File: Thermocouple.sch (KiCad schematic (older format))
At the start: 20 parts, among them P2 CONN_2, P3 CONN_3X2, U2 MCP3901, U3 LMT84, U4 OPA4170

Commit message: Terminal Blocks and ATX Connector
Created footprints for 12pin, 3pin terminal blocks and 24pin ATX Header.
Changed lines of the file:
@@
 	6700 4550 6200 4550
 Wire Wire Line
-	4300 3350 5300 3350
-Wire Wire Line
-	5300 3350 5450 3350
-Wire Wire Line
-	5300 2200 5300 3350
-Wire Wire Line
-	5300 3350 5300 3700
+	4300 3350 5450 3350
+Wire Wire Line
+	5300 2200 5300 3700
 Wire Wire Line
 	5700 2200 5300 2200
@@
 Connection ~ 7550 4550
 Wire Wire Line
-	8600 3650 8600 4200
-Wire Wire Line
-	8600 4200 8600 4450
+	8600 3650 8600 4450
 Wire Wire Line
 	7550 3650 8600 3650
@@
 	8600 3000 8600 2300
 Wire Wire Line
-	7550 3000 8250 3000
-Wire Wire Line
-	8250 3000 8600 3000
-Wire Wire Line
-	7200 2200 7550 2200
-Wire Wire Line
-	7550 2200 7600 2200
+	7550 3000 8600 3000
+Wire Wire Line
+	7200 2200 7600 2200
 Wire Wire Line
 	7550 2400 7550 2200
@@
 	7550 3650 7550 3750
 Wire Wire Line
-	7200 4550 7550 4550
-Wire Wire Line
-	7550 4550 7600 4550
+	7200 4550 7600 4550
 Wire Wire Line
 	7550 4250 7550 4550
@@
 $EndComp
 Wire Wire Line
-	5300 4100 5300 4550
-Wire Wire Line
-	5300 4550 5300 4700
+	5300 4100 5300 4700
 $Comp
 L AGND #PWR09
@@
 	8250 3350 8400 3350
 Wire Wire Line
-	8250 3000 8250 3250
-Wire Wire Line
-	8250 3250 8250 3350
-Wire Wire Line
-	8250 3350 8250 3450
+	8250 3000 8250 3450
 Connection ~ 8250 3000
 $Comp
@@
 	9550 4200 9550 4050
 Wire Wire Line
-	8600 4200 9300 4200
-Wire Wire Line
-	9300 4200 9550 4200
-Wire Wire Line
-	9550 4200 9800 4200
+	8600 4200 9800 4200
 Connection ~ 8600 4200
 Wire Wire Line
@@
 $EndComp
 Wire Wire Line
-	5950 6650 5950 6800
-Wire Wire Line
-	5950 6800 5950 6900
+	5950 6650 5950 6900
 Wire Wire Line
 	5850 6650 5850 6800
 Wire Wire Line
-	5850 6800 5950 6800
-Wire Wire Line
-	5950 6800 6050 6800
-Wire Wire Line
-	6050 6800 6550 6800
+	5850 6800 6550 6800
 Connection ~ 5950 6800
 Wire Wire Line
@@
 $EndComp
 Wire Wire Line
-	5900 5250 5900 5300
-Wire Wire Line
-	5900 5300 5900 5400
+	5900 5250 5900 5400
 $Comp
 L C C10
@@
 $EndComp
 Wire Wire Line
-	2950 1100 2950 1150
-Wire Wire Line
-	2950 1150 2950 1250
+	2950 1100 2950 1250
 Text GLabel 4450 1800 2    60   Input ~ 0
 REF+
@@
 $EndComp
 Wire Wire Line
-	2500 1100 2500 1150
-Wire Wire Line
-	2500 1150 2500 1250
+	2500 1100 2500 1250
 $Comp
 L C C6

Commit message: Layout v1.0
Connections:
- net +12V: no longer U4.4 (V+), U4.4 (V+), U4.4 (V+)
- net -12V: no longer U4.11 (V-), U4.11 (V-), U4.11 (V-)
- new net FE_V+: U4.4 (V+), U4.4 (V+), U4.4 (V+)
- new net FE_V-: U4.11 (V-), U4.11 (V-), U4.11 (V-)
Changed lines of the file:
@@
 Sheet 3 9
 Title ""
-Date "28 feb 2014"
+Date "3 mar 2014"
 Rev ""
 Comp ""
@@
 	8200 4950 8200 5050
 $Comp
-L +12V #PWR015
-U 1 1 530970D9
-P 8200 5050
-F 0 "#PWR015" H 8200 5000 20  0001 C CNN
-F 1 "+12V" H 8200 5150 30  0000 C CNN
-F 2 "" H 8200 5050 60  0000 C CNN
-F 3 "" H 8200 5050 60  0000 C CNN
-	1    8200 5050
-	-1   0    0    1
-$EndComp
-$Comp
-L +12V #PWR016
-U 1 1 530970DF
-P 6050 3850
-F 0 "#PWR016" H 6050 3800 20  0001 C CNN
-F 1 "+12V" H 6050 3950 30  0000 C CNN
-F 2 "" H 6050 3850 60  0000 C CNN
-F 3 "" H 6050 3850 60  0000 C CNN
-	1    6050 3850
-	-1   0    0    1
-$EndComp
-$Comp
-L +12V #PWR017
-U 1 1 530970E5
-P 8200 1700
-F 0 "#PWR017" H 8200 1650 20  0001 C CNN
-F 1 "+12V" H 8200 1800 30  0000 C CNN
-F 2 "" H 8200 1700 60  0000 C CNN
-F 3 "" H 8200 1700 60  0000 C CNN
-	1    8200 1700
-	1    0    0    -1
-$EndComp
-$Comp
-L -12V #PWR018
-U 1 1 530970EB
-P 8200 4050
-F 0 "#PWR018" H 8200 4180 20  0001 C CNN
-F 1 "-12V" H 8200 4150 30  0000 C CNN
-F 2 "" H 8200 4050 60  0000 C CNN
-F 3 "" H 8200 4050 60  0000 C CNN
-	1    8200 4050
-	1    0    0    -1
-$EndComp
-$Comp
-L -12V #PWR019
-U 1 1 530970F1
-P 6050 2850
-F 0 "#PWR019" H 6050 2980 20  0001 C CNN
-F 1 "-12V" H 6050 2950 30  0000 C CNN
-F 2 "" H 6050 2850 60  0000 C CNN
-F 3 "" H 6050 2850 60  0000 C CNN
-	1    6050 2850
-	1    0    0    -1
-$EndComp
-$Comp
-L -12V #PWR020
-U 1 1 530970F7
-P 8200 2700
-F 0 "#PWR020" H 8200 2830 20  0001 C CNN
-F 1 "-12V" H 8200 2800 30  0000 C CNN
-F 2 "" H 8200 2700 60  0000 C CNN
-F 3 "" H 8200 2700 60  0000 C CNN
-	1    8200 2700
-	-1   0    0    1
-$EndComp
-$Comp
 L C C9
 U 1 1 530970FD
@@
 	6550 5300 6550 5850
 $Comp
-L +5V #PWR021
+L +5V #PWR015
 U 1 1 53097117
 P 2950 1100
-F 0 "#PWR021" H 2950 1190 20  0001 C CNN
+F 0 "#PWR015" H 2950 1190 20  0001 C CNN
 F 1 "+5V" H 2950 1190 30  0000 C CNN
 F 2 "" H 2950 1100 60  0000 C CNN
@@
 Connection ~ 2950 1150
 $Comp
-L AGND #PWR022
+L AGND #PWR016
 U 1 1 530972DF
 P 3550 1250
-F 0 "#PWR022" H 3550 1250 40  0001 C CNN
+F 0 "#PWR016" H 3550 1250 40  0001 C CNN
 F 1 "AGND" H 3550 1180 50  0000 C CNN
 F 2 "" H 3550 1250 60  0000 C CNN
@@
 	3550 1150 3450 1150
 $Comp
-L +5V #PWR023
+L +5V #PWR017
 U 1 1 5309733E
 P 2500 1100
-F 0 "#PWR023" H 2500 1190 20  0001 C CNN
+F 0 "#PWR017" H 2500 1190 20  0001 C CNN
 F 1 "+5V" H 2500 1190 30  0000 C CNN
 F 2 "" H 2500 1100 60  0000 C CNN
@@
 Connection ~ 2500 1150
 $Comp
-L AGND #PWR024
+L AGND #PWR018
 U 1 1 5309734D
 P 1900 1250
-F 0 "#PWR024" H 1900 1250 40  0001 C CNN
+F 0 "#PWR018" H 1900 1250 40  0001 C CNN
 F 1 "AGND" H 1900 1180 50  0000 C CNN
 F 2 "" H 1900 1250 60  0000 C CNN
@@
 	2500 5100 2500 5250
 $Comp
-L AGND #PWR025
+L AGND #PWR019
 U 1 1 530973B4
 P 2500 5250
-F 0 "#PWR025" H 2500 5250 40  0001 C CNN
+F 0 "#PWR019" H 2500 5250 40  0001 C CNN
 F 1 "AGND" H 2500 5180 50  0000 C CNN
 F 2 "" H 2500 5250 60  0000 C CNN
@@
 Wire Wire Line
 	1300 4500 1400 4500
+$Comp
+L FE_V- #PWR16
+U 1 1 5312A19A
+P 6050 2850
+F 0 "#PWR16" H 6050 3050 40  0001 C CNN
+F 1 "FE_V-" H 6050 3000 40  0000 C CNN
+F 2 "" H 6050 2850 60  0000 C CNN
+F 3 "" H 6050 2850 60  0000 C CNN
+	1    6050 2850
+	1    0    0    -1
+$EndComp
+$Comp
+L FE_V+ #PWR020
+U 1 1 5312A1A0
+P 6050 3850
+F 0 "#PWR020" H 6050 3950 30  0001 C CNN
+F 1 "FE_V+" H 6050 3950 30  0000 C CNN
+F 2 "" H 6050 3850 60  0000 C CNN
+F 3 "" H 6050 3850 60  0000 C CNN
+	1    6050 3850
+	-1   0    0    1
+$EndComp
+$Comp
+L FE_V- #PWR20
+U 1 1 5312A1BA
+P 8200 4050
+F 0 "#PWR20" H 8200 4250 40  0001 C CNN
+F 1 "FE_V-" H 8200 4200 40  0000 C CNN
+F 2 "" H 8200 4050 60  0000 C CNN
+F 3 "" H 8200 4050 60  0000 C CNN
+	1    8200 4050
+	1    0    0    -1
+$EndComp
+$Comp
+L FE_V+ #PWR021
+U 1 1 5312A1C0
+P 8200 5050
+F 0 "#PWR021" H 8200 5150 30  0001 C CNN
+F 1 "FE_V+" H 8200 5150 30  0000 C CNN
+F 2 "" H 8200 5050 60  0000 C CNN
+F 3 "" H 8200 5050 60  0000 C CNN
+	1    8200 5050
+	-1   0    0    1
+$EndComp
+$Comp
+L FE_V- #PWR19
+U 1 1 5312A1C6
+P 8200 2700
+F 0 "#PWR19" H 8200 2900 40  0001 C CNN
+F 1 "FE_V-" H 8200 2850 40  0000 C CNN
+F 2 "" H 8200 2700 60  0000 C CNN
+F 3 "" H 8200 2700 60  0000 C CNN
+	1    8200 2700
+	-1   0    0    1
+$EndComp
+$Comp
+L FE_V+ #PWR022
+U 1 1 5312A1D1
+P 8200 1700
+F 0 "#PWR022" H 8200 1800 30  0001 C CNN
+F 1 "FE_V+" H 8200 1800 30  0000 C CNN
+F 2 "" H 8200 1700 60  0000 C CNN
+F 3 "" H 8200 1700 60  0000 C CNN
+	1    8200 1700
+	1    0    0    -1
+$EndComp
 $EndSCHEMATC

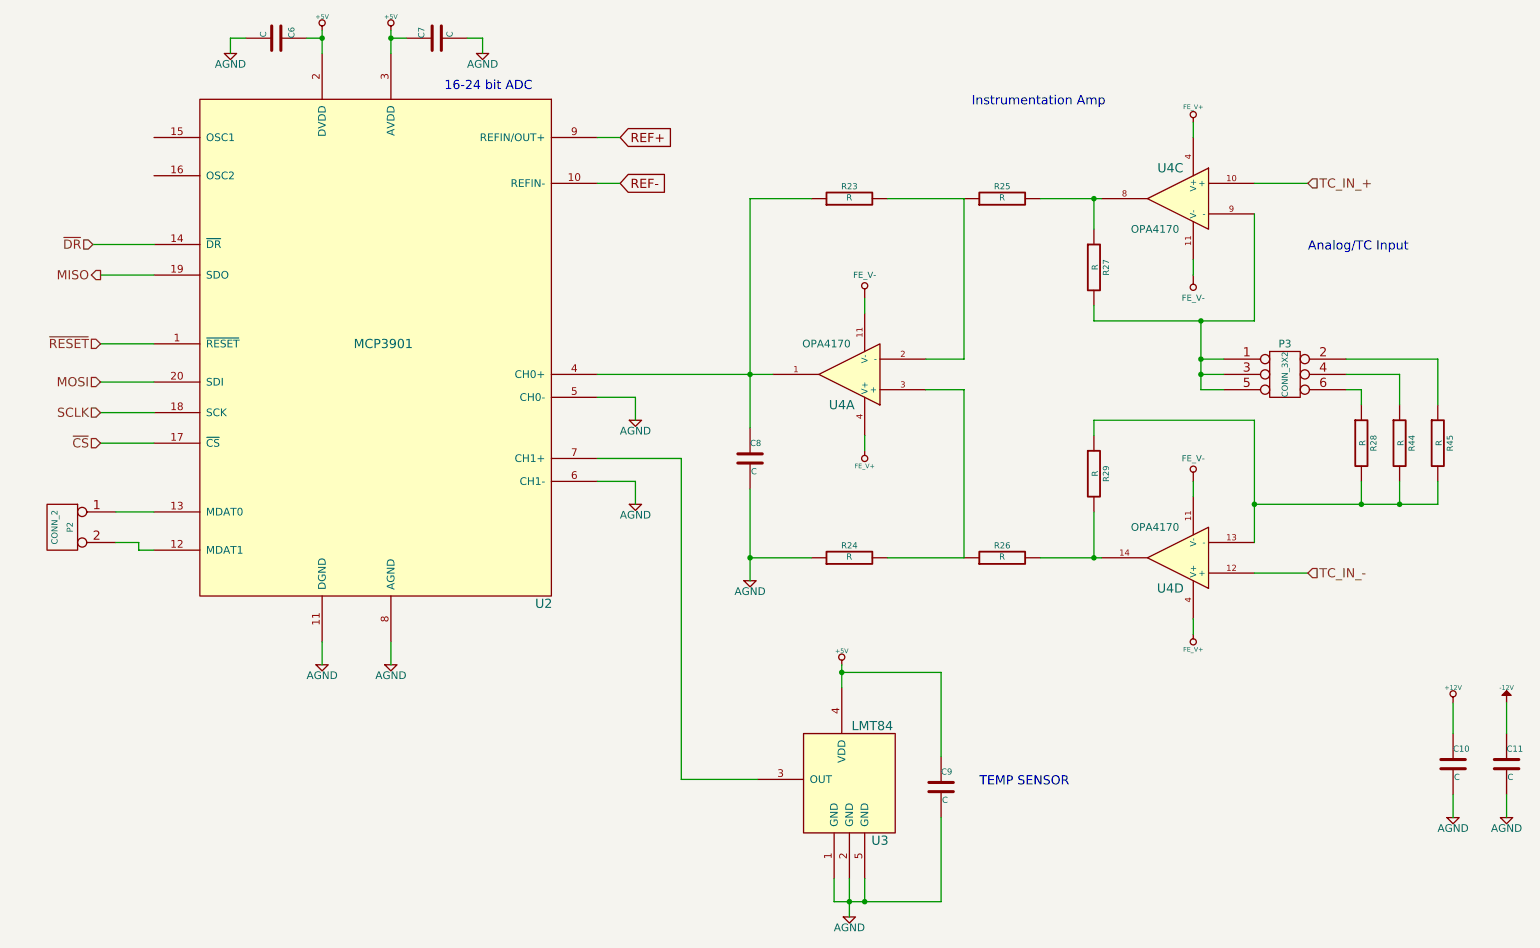
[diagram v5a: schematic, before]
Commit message: Layout v4.0
Adding ground planes according to location of modules
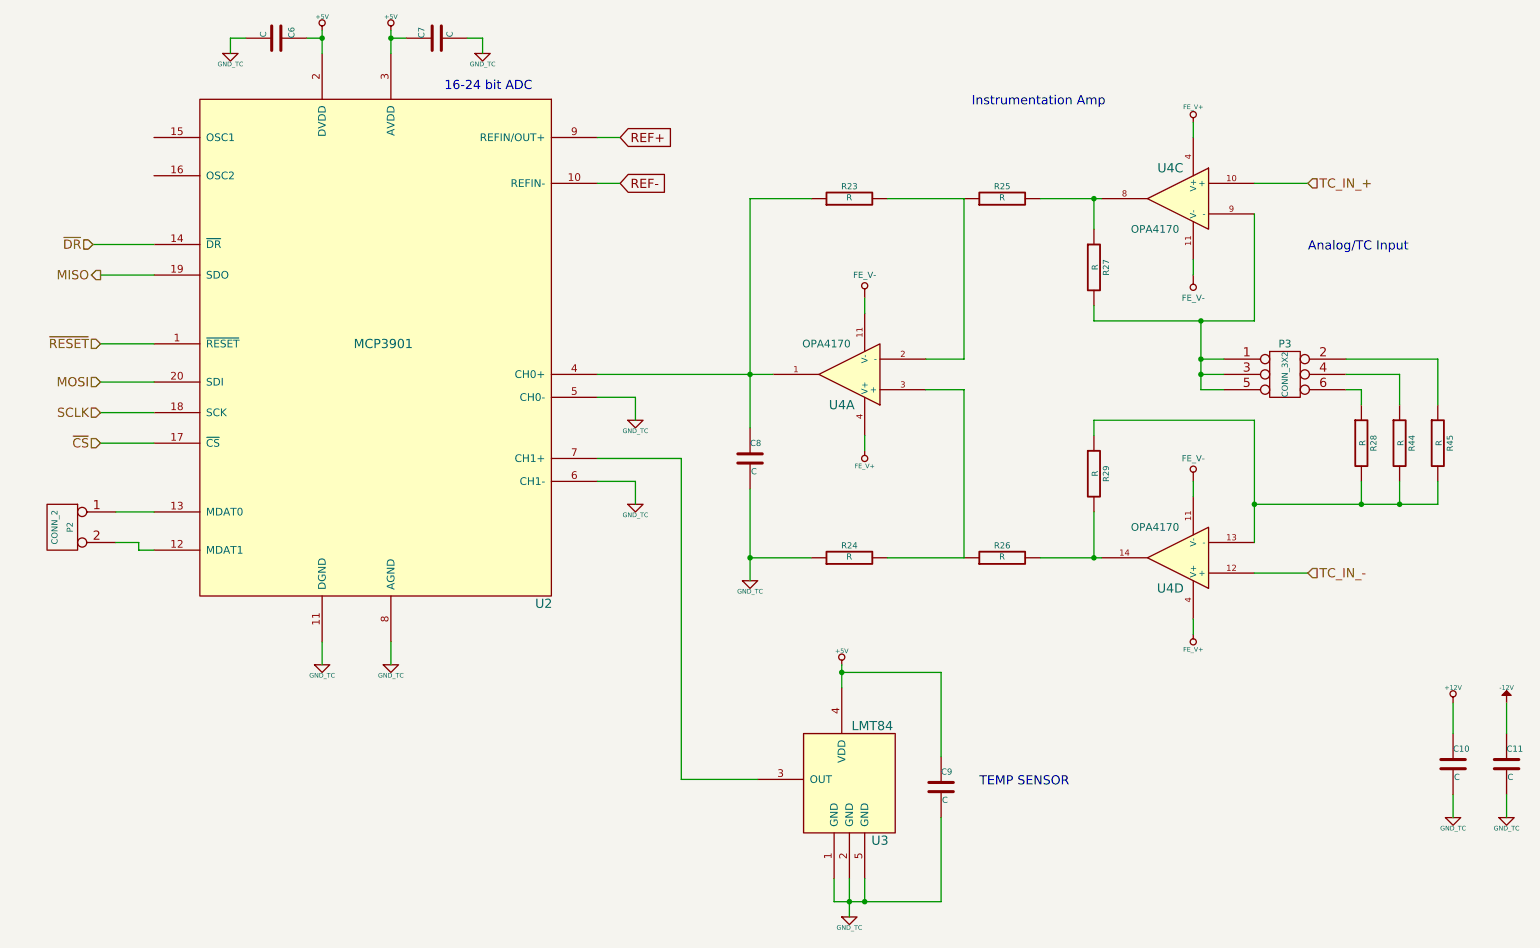
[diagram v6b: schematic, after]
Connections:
- net AGND renamed GND_TC

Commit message: Layout v5.0
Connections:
- net GND_TC renamed AGND
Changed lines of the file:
@@
 Sheet 3 9
 Title ""
-Date "6 mar 2014"
+Date "8 mar 2014"
 Rev ""
 Comp ""
@@
 $EndComp
 $Comp
-L GND_TC #PWR013
-U 1 1 531835B4
-P 2500 5250
-F 0 "#PWR013" H 2500 5250 30  0001 C CNN
-F 1 "GND_TC" H 2500 5180 30  0000 C CNN
-F 2 "" H 2500 5250 60  0000 C CNN
-F 3 "" H 2500 5250 60  0000 C CNN
-	1    2500 5250
-	1    0    0    -1
-$EndComp
-$Comp
-L GND_TC #PWR014
-U 1 1 531835C3
-P 2950 5250
-F 0 "#PWR014" H 2950 5250 30  0001 C CNN
-F 1 "GND_TC" H 2950 5180 30  0000 C CNN
-F 2 "" H 2950 5250 60  0000 C CNN
-F 3 "" H 2950 5250 60  0000 C CNN
-	1    2950 5250
-	1    0    0    -1
-$EndComp
-$Comp
-L GND_TC #PWR015
-U 1 1 531835D2
-P 5950 6900
-F 0 "#PWR015" H 5950 6900 30  0001 C CNN
-F 1 "GND_TC" H 5950 6830 30  0000 C CNN
-F 2 "" H 5950 6900 60  0000 C CNN
-F 3 "" H 5950 6900 60  0000 C CNN
-	1    5950 6900
-	1    0    0    -1
-$EndComp
-$Comp
-L GND_TC #PWR016
-U 1 1 531835E1
-P 9900 6250
-F 0 "#PWR016" H 9900 6250 30  0001 C CNN
-F 1 "GND_TC" H 9900 6180 30  0000 C CNN
-F 2 "" H 9900 6250 60  0000 C CNN
-F 3 "" H 9900 6250 60  0000 C CNN
-	1    9900 6250
-	1    0    0    -1
-$EndComp
-$Comp
-L GND_TC #PWR017
-U 1 1 531835F0
-P 10250 6250
-F 0 "#PWR017" H 10250 6250 30  0001 C CNN
-F 1 "GND_TC" H 10250 6180 30  0000 C CNN
-F 2 "" H 10250 6250 60  0000 C CNN
-F 3 "" H 10250 6250 60  0000 C CNN
-	1    10250 6250
-	1    0    0    -1
-$EndComp
-$Comp
-L GND_TC #PWR018
-U 1 1 531835FF
-P 5300 4700
-F 0 "#PWR018" H 5300 4700 30  0001 C CNN
-F 1 "GND_TC" H 5300 4630 30  0000 C CNN
-F 2 "" H 5300 4700 60  0000 C CNN
-F 3 "" H 5300 4700 60  0000 C CNN
-	1    5300 4700
-	1    0    0    -1
-$EndComp
-$Comp
-L GND_TC #PWR019
-U 1 1 5318360E
-P 4550 4200
-F 0 "#PWR019" H 4550 4200 30  0001 C CNN
-F 1 "GND_TC" H 4550 4130 30  0000 C CNN
-F 2 "" H 4550 4200 60  0000 C CNN
-F 3 "" H 4550 4200 60  0000 C CNN
-	1    4550 4200
-	1    0    0    -1
-$EndComp
-$Comp
-L GND_TC #PWR020
-U 1 1 5318361D
-P 4550 3650
-F 0 "#PWR020" H 4550 3650 30  0001 C CNN
-F 1 "GND_TC" H 4550 3580 30  0000 C CNN
-F 2 "" H 4550 3650 60  0000 C CNN
-F 3 "" H 4550 3650 60  0000 C CNN
-	1    4550 3650
-	1    0    0    -1
-$EndComp
-$Comp
 L MCP3901 U2
 U 1 1 53095B8E
@@
 $EndComp
 $Comp
-L GND_TC #PWR021
-U 1 1 5318362C
+L AGND #PWR013
+U 1 1 53198D6E
+P 5950 6900
+F 0 "#PWR013" H 5950 6900 40  0001 C CNN
+F 1 "AGND" H 5950 6830 50  0000 C CNN
+F 2 "" H 5950 6900 60  0000 C CNN
+F 3 "" H 5950 6900 60  0000 C CNN
+	1    5950 6900
+	1    0    0    -1
+$EndComp
+$Comp
+L AGND #PWR014
+U 1 1 53198D7D
+P 5300 4700
+F 0 "#PWR014" H 5300 4700 40  0001 C CNN
+F 1 "AGND" H 5300 4630 50  0000 C CNN
+F 2 "" H 5300 4700 60  0000 C CNN
+F 3 "" H 5300 4700 60  0000 C CNN
+	1    5300 4700
+	1    0    0    -1
+$EndComp
+$Comp
+L AGND #PWR015
+U 1 1 53198D8C
+P 4550 4200
+F 0 "#PWR015" H 4550 4200 40  0001 C CNN
+F 1 "AGND" H 4550 4130 50  0000 C CNN
+F 2 "" H 4550 4200 60  0000 C CNN
+F 3 "" H 4550 4200 60  0000 C CNN
+	1    4550 4200
+	1    0    0    -1
+$EndComp
+$Comp
+L AGND #PWR016
+U 1 1 53198D9B
+P 4550 3650
+F 0 "#PWR016" H 4550 3650 40  0001 C CNN
+F 1 "AGND" H 4550 3580 50  0000 C CNN
+F 2 "" H 4550 3650 60  0000 C CNN
+F 3 "" H 4550 3650 60  0000 C CNN
+	1    4550 3650
+	1    0    0    -1
+$EndComp
+$Comp
+L AGND #PWR017
+U 1 1 53198DAA
+P 2500 5250
+F 0 "#PWR017" H 2500 5250 40  0001 C CNN
+F 1 "AGND" H 2500 5180 50  0000 C CNN
+F 2 "" H 2500 5250 60  0000 C CNN
+F 3 "" H 2500 5250 60  0000 C CNN
+	1    2500 5250
+	1    0    0    -1
+$EndComp
+$Comp
+L AGND #PWR018
+U 1 1 53198DB9
+P 2950 5250
+F 0 "#PWR018" H 2950 5250 40  0001 C CNN
+F 1 "AGND" H 2950 5180 50  0000 C CNN
+F 2 "" H 2950 5250 60  0000 C CNN
+F 3 "" H 2950 5250 60  0000 C CNN
+	1    2950 5250
+	1    0    0    -1
+$EndComp
+$Comp
+L AGND #PWR019
+U 1 1 53198DC8
 P 1900 1250
-F 0 "#PWR021" H 1900 1250 30  0001 C CNN
-F 1 "GND_TC" H 1900 1180 30  0000 C CNN
+F 0 "#PWR019" H 1900 1250 40  0001 C CNN
+F 1 "AGND" H 1900 1180 50  0000 C CNN
 F 2 "" H 1900 1250 60  0000 C CNN
 F 3 "" H 1900 1250 60  0000 C CNN
@@
 $EndComp
 $Comp
-L GND_TC #PWR022
-U 1 1 5318363B
+L AGND #PWR020
+U 1 1 53198DD7
 P 3550 1250
-F 0 "#PWR022" H 3550 1250 30  0001 C CNN
-F 1 "GND_TC" H 3550 1180 30  0000 C CNN
+F 0 "#PWR020" H 3550 1250 40  0001 C CNN
+F 1 "AGND" H 3550 1180 50  0000 C CNN
 F 2 "" H 3550 1250 60  0000 C CNN
 F 3 "" H 3550 1250 60  0000 C CNN
@@
 	1    0    0    -1
 $EndComp
+$Comp
+L AGND #PWR021
+U 1 1 53198DE6
+P 9900 6250
+F 0 "#PWR021" H 9900 6250 40  0001 C CNN
+F 1 "AGND" H 9900 6180 50  0000 C CNN
+F 2 "" H 9900 6250 60  0000 C CNN
+F 3 "" H 9900 6250 60  0000 C CNN
+	1    9900 6250
+	1    0    0    -1
+$EndComp
+$Comp
+L AGND #PWR022
+U 1 1 53198DF5
+P 10250 6250
+F 0 "#PWR022" H 10250 6250 40  0001 C CNN
+F 1 "AGND" H 10250 6180 50  0000 C CNN
+F 2 "" H 10250 6250 60  0000 C CNN
+F 3 "" H 10250 6250 60  0000 C CNN
+	1    10250 6250
+	1    0    0    -1
+$EndComp
